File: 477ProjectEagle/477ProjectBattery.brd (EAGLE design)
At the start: 100 x 80 mm, 21 parts

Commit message: Minor changes to battery PCB
Changed board size. Fixed acute angle. Fixed a polygon or two
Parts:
- moved CIN 26.3 mm to (9.93, 28.9)
- moved COUT 26.3 mm to (15.0, 31.6)
- moved L1 26.3 mm to (22.4, 30.1)
- moved U$11 26.3 mm to (36.4, 23.0)
- moved U$12 26.3 mm to (14.7, 27.8)
- moved U$4 26.3 mm to (11.3, 41.6)
- moved U$6 26.3 mm to (27.5, 42.0)
- moved U$7 26.3 mm to (15.1, 39.2)
- moved U$9 26.3 mm to (41.2, 38.5)
- moved - 26.3 mm to (30.9, 14.4)
- moved -- 26.3 mm to (38.6, 14.5)
- moved .. 26.3 mm to (22.6, 14.6)
- moved R1 26.3 mm to (21.4, 23.7)
- moved R2 26.3 mm to (15.0, 24.0)
- moved R3 26.3 mm to (18.5, 35.4)
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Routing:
- net N$1: track 26.4 -> 24.5 mm
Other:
- board size 100 x 80 mm -> 50.8 x 50.8 mm

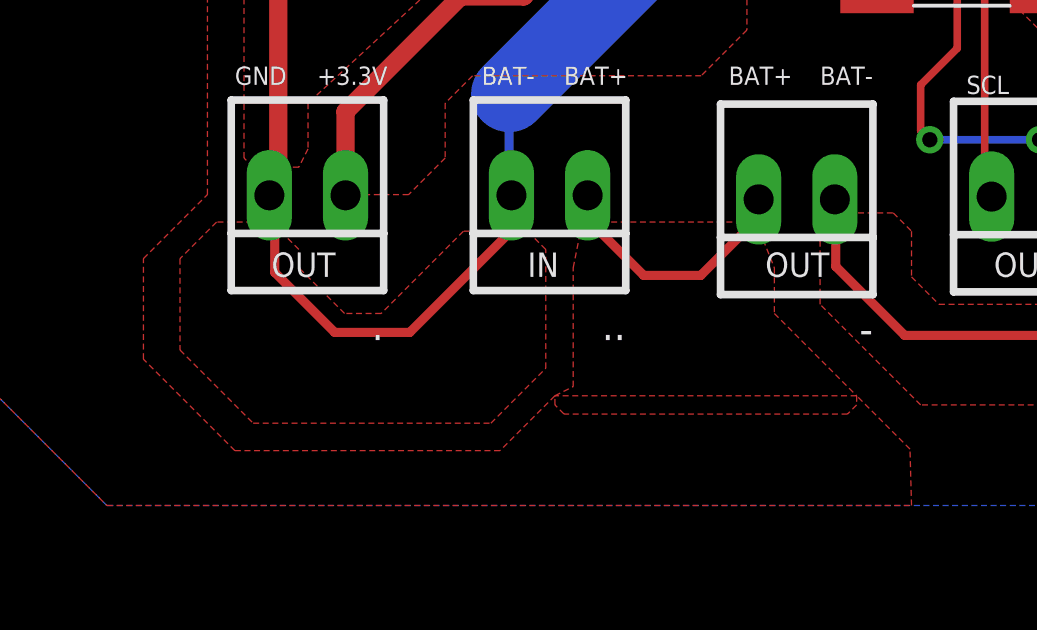
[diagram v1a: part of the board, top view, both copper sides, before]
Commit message: Fixed thermals and traces on RJ-11 connector
Scott Lab
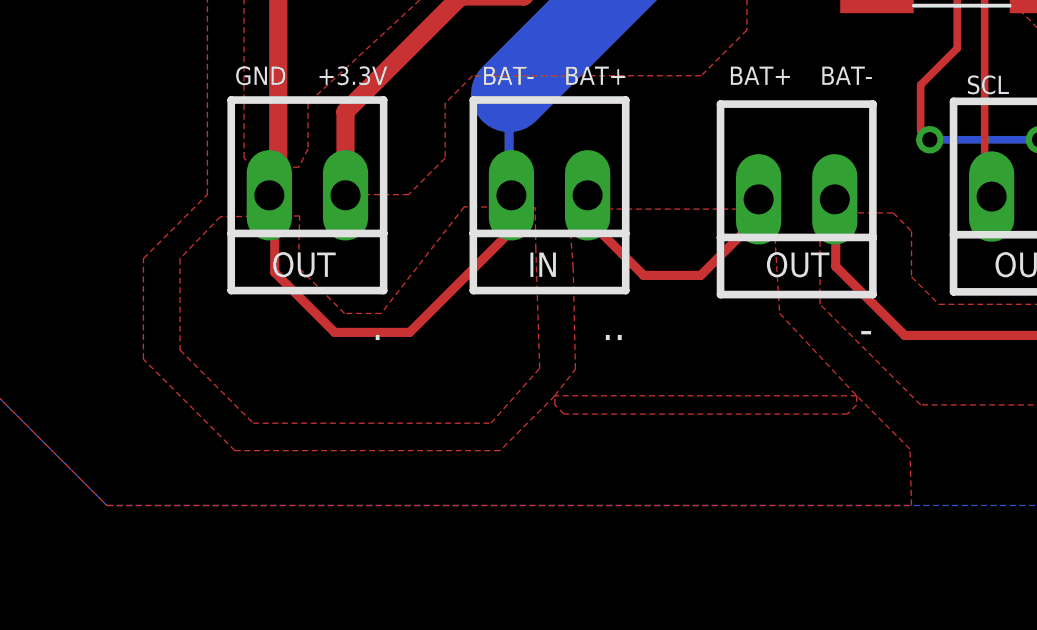
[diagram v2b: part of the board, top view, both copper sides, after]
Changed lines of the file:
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@@
 <wire x1="9.798" y1="41.486" x2="9.908" y2="41.596" width="0.3048" layer="1"/>
 <polygon width="0.3048" layer="1" thermals="no">
-<vertex x="23.7236" y="13.6652"/>
-<vertex x="29.5148" y="13.6652"/>
-<vertex x="30.1244" y="12.1412"/>
-<vertex x="30.1244" y="10.6172"/>
+<vertex x="23.2664" y="14.097"/>
+<vertex x="30.099" y="14.097"/>
+<vertex x="30.2006" y="12.192"/>
+<vertex x="30.3022" y="10.6172"/>
 <vertex x="32.8676" y="7.874"/>
 <vertex x="32.8676" y="7.5692"/>
@@
 <vertex x="22.8092" y="7.5692"/>
 <vertex x="22.8092" y="7.874"/>
-<vertex x="23.4188" y="8.1788"/>
+<vertex x="23.495" y="8.763"/>
 <vertex x="23.4188" y="12.1412"/>
 </polygon>
@@
 <wire x1="15.47" y1="9.986" x2="13.47" y2="11.986" width="0.3048" layer="1"/>
 <wire x1="13.47" y1="11.986" x2="13.47" y2="13.486" width="0.3048" layer="1"/>
-<wire x1="13.47" y1="13.486" x2="13.57" y2="13.586" width="0.3048" layer="1"/>
-<wire x1="13.57" y1="13.586" x2="13.47" y2="13.586" width="0.3048" layer="1"/>
+<wire x1="13.47" y1="13.486" x2="13.5192" y2="13.459" width="0.3048" layer="1"/>
+<wire x1="13.5192" y1="13.459" x2="13.47" y2="13.586" width="0.3048" layer="1"/>
 <wire x1="13.47" y1="13.586" x2="13.37" y2="13.486" width="0.3048" layer="1"/>
 <wire x1="13.588" y1="24.026" x2="13.588" y2="15.604" width="0.6096" layer="1"/>
@@
 </polygon>
 <polygon width="0.3048" layer="1" thermals="no">
-<vertex x="13.3604" y="13.6652"/>
-<vertex x="11.5316" y="13.6652"/>
+<vertex x="14.3002" y="13.8684"/>
+<vertex x="11.6586" y="13.843"/>
 <vertex x="10.3124" y="12.446"/>
 <vertex x="10.3124" y="9.398"/>
 <vertex x="12.7508" y="6.9596"/>
 <vertex x="20.6756" y="6.9596"/>
-<vertex x="22.5044" y="8.7884"/>
-<vertex x="22.5044" y="12.7508"/>
-<vertex x="21.8948" y="13.3604"/>
-<vertex x="19.7612" y="13.3604"/>
+<vertex x="22.3012" y="8.7884"/>
+<vertex x="22.1742" y="12.7508"/>
+<vertex x="22.1488" y="14.1478"/>
+<vertex x="19.7866" y="14.1732"/>
 <vertex x="17.018" y="10.6172"/>
 <vertex x="15.7988" y="10.6172"/>
@@
 <vertex x="14.2748" y="12.7508"/>
 </polygon>
-<polygon width="0.3048" layer="16">
+<polygon width="0.3048" layer="16" thermals="no">
 <vertex x="7.874" y="46.2788"/>
 <vertex x="45.3644" y="46.2788"/>

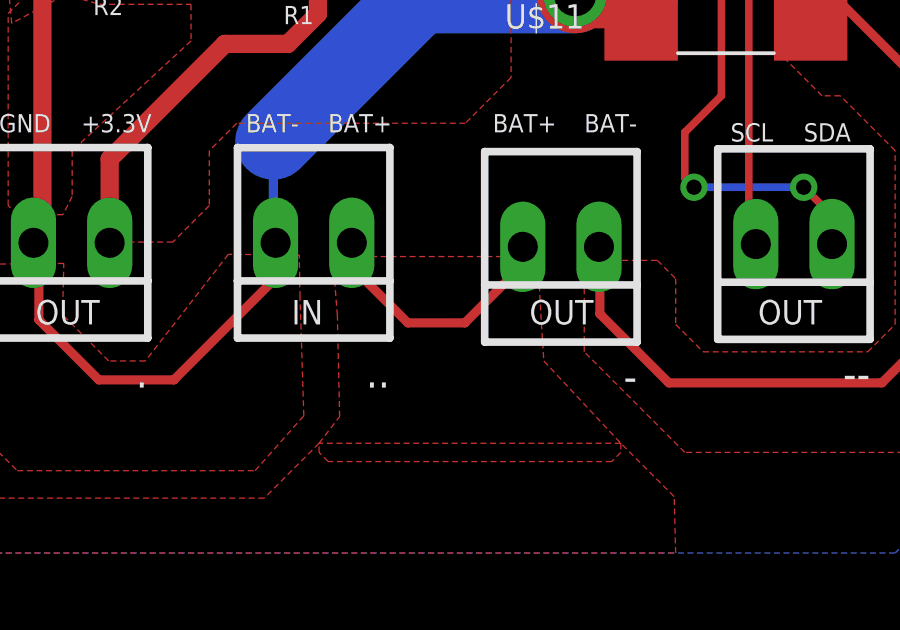
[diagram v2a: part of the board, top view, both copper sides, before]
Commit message: Fixed Schematic to include cap for internal reg
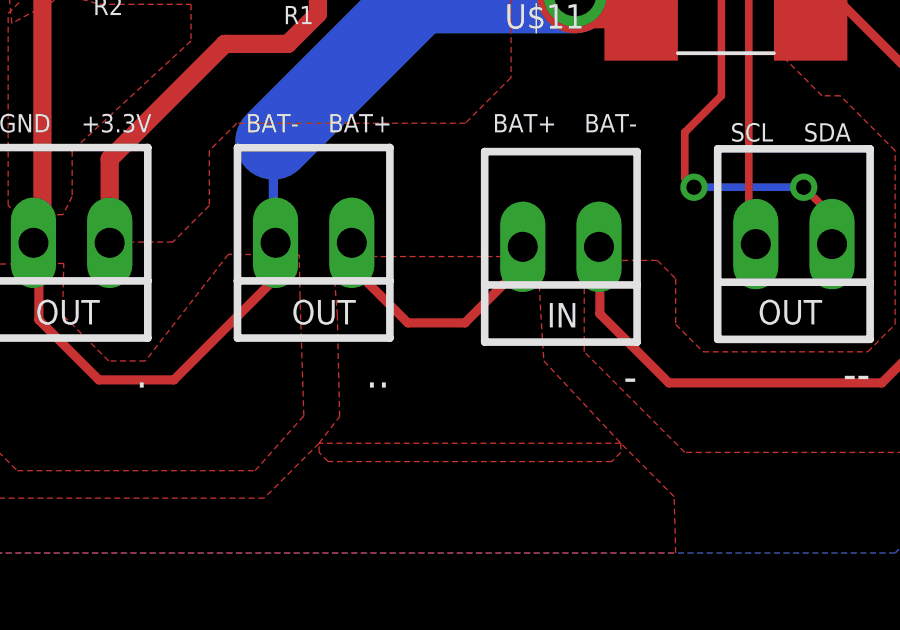
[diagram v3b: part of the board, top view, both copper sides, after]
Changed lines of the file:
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@@
 <wire x1="0" y1="50.8" x2="0" y2="0" width="0" layer="20"/>
 <text x="13.3604" y="11.8364" size="0.8128" layer="21" ratio="15">OUT</text>
-<text x="29.8196" y="11.8364" size="0.8128" layer="21" ratio="15">OUT</text>
+<text x="30.4038" y="11.7348" size="0.8128" layer="21" ratio="15">IN</text>
 <text x="37.4396" y="11.8364" size="0.8128" layer="21" ratio="15">OUT</text>
-<text x="21.8948" y="11.8364" size="0.8128" layer="21" ratio="15">IN</text>
+<text x="21.8948" y="11.8364" size="0.8128" layer="21" ratio="15">OUT</text>
 <text x="14.8844" y="18.2372" size="0.6096" layer="21" ratio="15">+3.3V</text>
 <text x="12.1412" y="18.2372" size="0.6096" layer="21" ratio="15">GND</text>

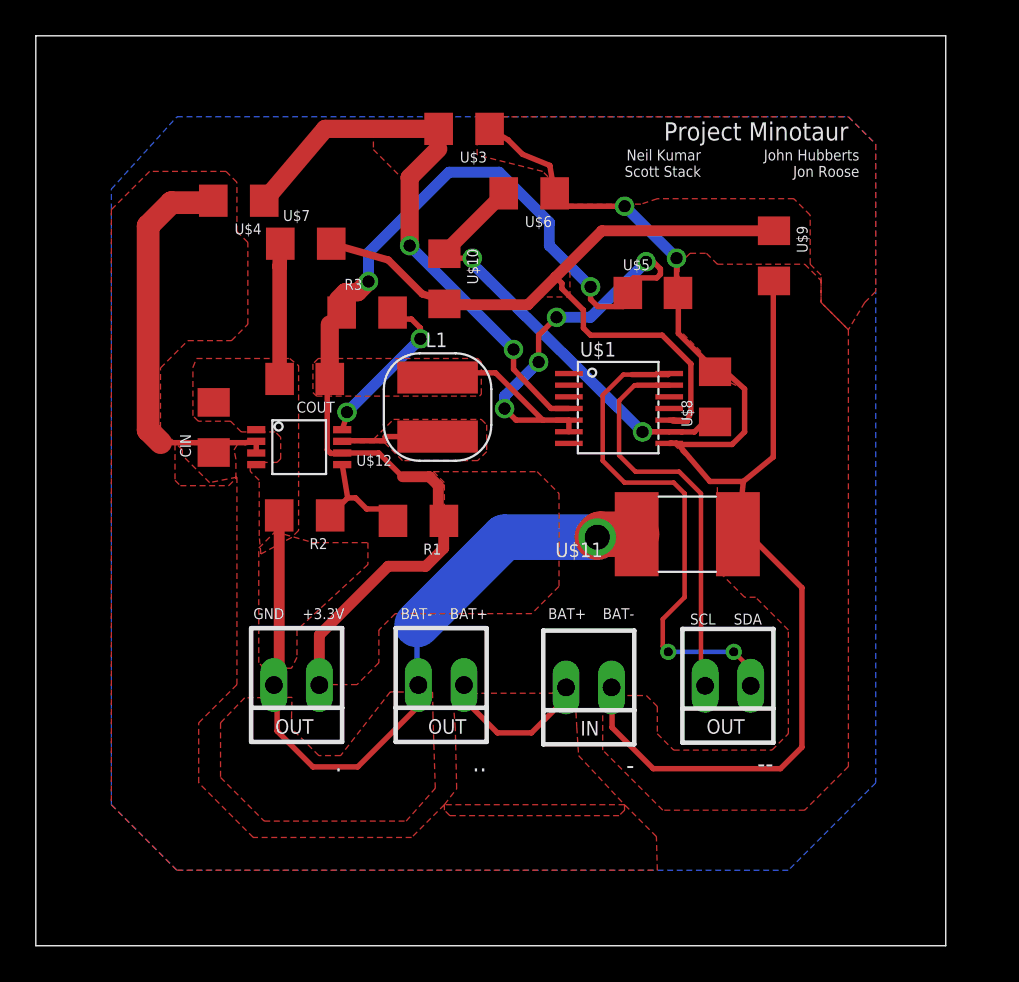
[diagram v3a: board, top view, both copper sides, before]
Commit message: PCB is almost finalized.
Scott Lab- Added bulk cap. added GND plane. Added lots of information on
the silkscreen. Barrel connectors for all power sources. Verified and
fixed programming header(added cap). Added barrel connectors to battery
PCB and made standoff drill holes.
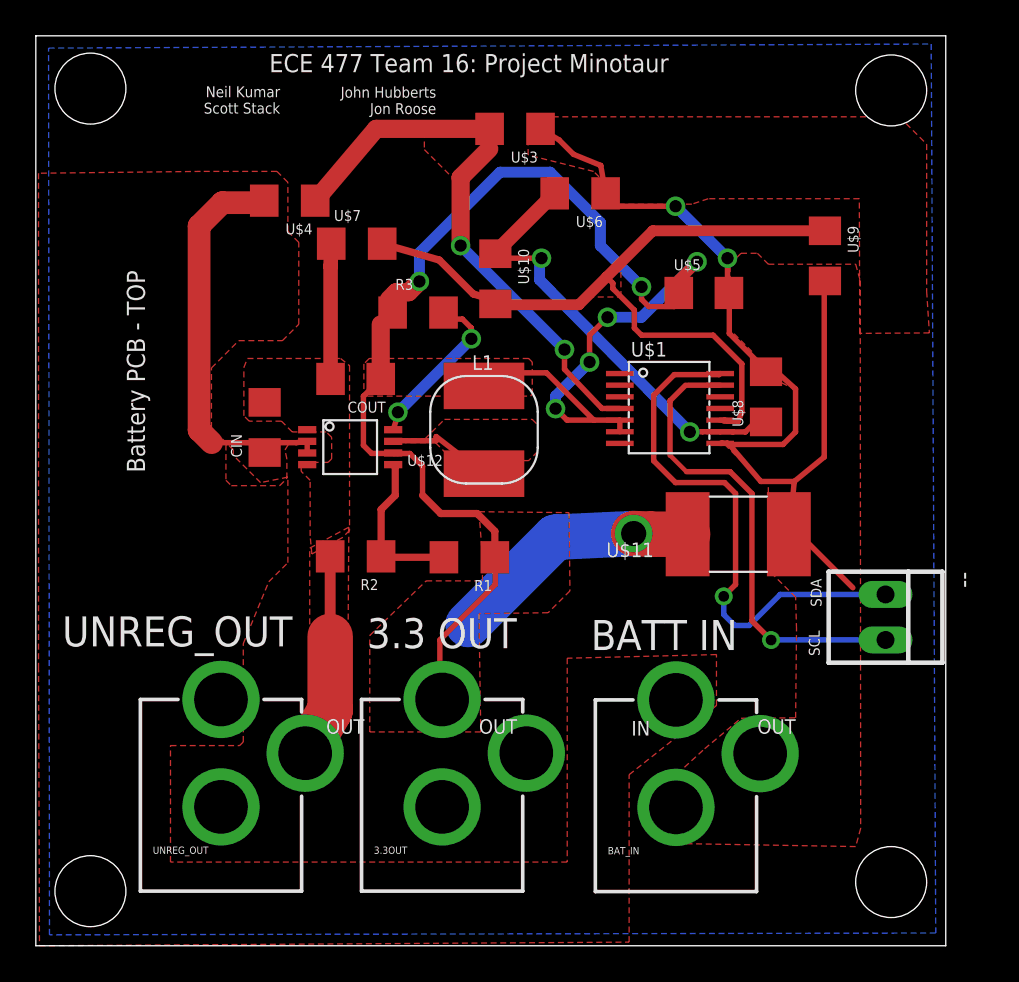
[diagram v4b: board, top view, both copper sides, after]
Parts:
- removed -, ., ..: (no value), con-molex:22-23-2021
- added 3.3OUT, BAT_IN, UNREG_OUT: POWER_JACKPTH, SparkFun-Connectors:POWER_JACK_PTH
- moved -- 9.60 mm to (47.4, 18.3), turned to 270 degrees
- moved R2 3.65 mm to (17.9, 21.7)
- moved R1 3.50 mm to (24.2, 21.7)
- moved L1 2.89 mm to (25.0, 28.8)
- moved U$11 2.84 mm to (39.2, 23.0)
- moved U$10 2.84 mm to (25.7, 37.2)
- moved CIN 2.84 mm to (12.8, 28.9)
- moved COUT 2.84 mm to (17.9, 31.6)
- moved U$12 2.84 mm to (17.6, 27.8)
- moved R3 2.84 mm to (21.3, 35.4)
- moved U$1 2.84 mm to (35.4, 30.0)
- moved U$3 2.84 mm to (26.8, 45.6)
- moved U$4 2.84 mm to (14.2, 41.6)
- moved U$5 2.84 mm to (37.3, 36.4)
- moved U$6 2.84 mm to (30.4, 42.0)
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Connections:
- net +3V3: now also 3.3OUT.PWR; no longer ..1
- net GND: now also BAT_IN.GND, BAT_IN.GNDBREAK; no longer -.1
- net GNDA: now also 3.3OUT.GND, 3.3OUT.GNDBREAK, UNREG_OUT.GND, UNREG_OUT.GNDBREAK; no longer ...2, ..2
- net N$4: now also BAT_IN.PWR, UNREG_OUT.PWR; no longer -.2, ...1
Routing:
- net GND: track 79.0 -> 56.5 mm
- net GNDA: track 47.0 -> 35.0 mm
- net N$4: track 32.9 -> 24.2 mm
- net N$5: track 22.5 -> 26.7 mm, vias 0 -> 1
- net N$40: track 6.44 -> 9.02 mm
- net N$6: track 28.6 -> 30.2 mm, vias 2 -> 1
- net +3V3: track 88.4 -> 86.8 mm
- net N$1: track 24.5 -> 25.1 mm
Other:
- board text added: "3.3 OUT"
- board text added: "BATT IN"
- board text added: "Battery PCB - TOP"
- board text added: "ECE 477 Team 16: Project Minotaur"
- board text added: "UNREG_OUT"
- board text removed: "+3.3V"
- board text removed: "BAT+"
- board text removed: "BAT-"
- board text removed: "GND"
- board text removed: "Project Minotaur"

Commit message: Finishing touches on PCB
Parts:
- added U$2: 1uF, MinotaurParts:C1206
- U$3: value 16k -> 16.5k
- U$4: value 240k -> 255k
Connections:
- new net N$7: U$1.7, U$2.1
- net GND: now also U$1.1, U$1.3, U$2.2
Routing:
- net GND: track 56.5 -> 87.7 mm, vias 2 -> 4
- net +3V3: track 86.8 -> 57.0 mm, vias 6 -> 4
- net N$7: track 0.00 -> 4.10 mm
- net N$1: track 25.1 -> 25.7 mm
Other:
- board text added: "PCB 2 of 2 TOP"
- board text removed: "Battery PCB - TOP"
